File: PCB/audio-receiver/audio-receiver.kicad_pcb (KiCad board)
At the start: 2 copper layers, 143.5 x 71.5 mm, 74 parts, among them J1 Screw_Terminal_01x03, J2 Screw_Terminal_01x04, J3 Screw_Terminal_01x02, Q1 BC559, Q10 BD140, Q11 MJE3055, Q12 MJE2955, Q2 BD139, Q3 BD139, Q4 BD140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

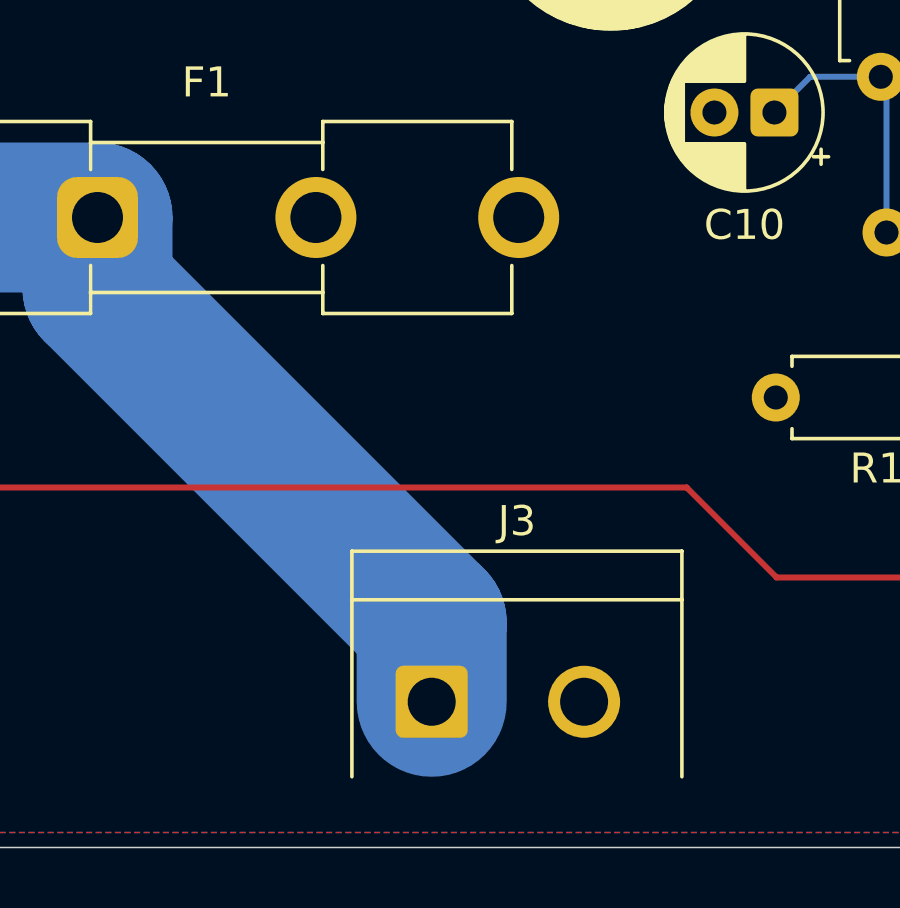
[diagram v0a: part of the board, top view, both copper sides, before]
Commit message: improve current handling of pcb
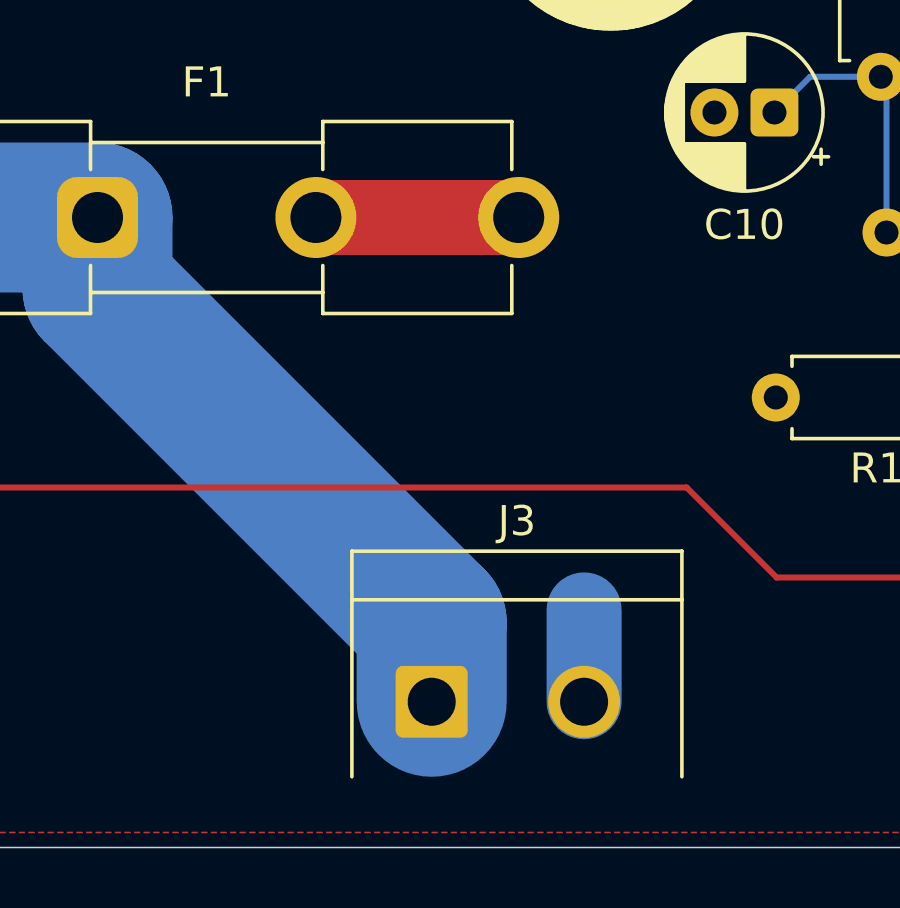
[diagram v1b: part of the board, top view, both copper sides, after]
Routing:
- net VCC: track 1.89 -> 8.65 mm
- net GND: track 6.10 -> 9.16 mm
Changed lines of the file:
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@@
+	)
+	(segment
+		(start 144.58 128.1425)
+		(end 144.58 125.08)
+		(width 2.5)
+		(layer "B.Cu")
+		(net 11)
 	)
 	(segment
@@
 		(layer "F.Cu")
 		(net 13)
+	)
+	(segment
+		(start 135.64 112)
+		(end 142.4 112)
+		(width 2.5)
+		(layer "F.Cu")
+		(net 13)
